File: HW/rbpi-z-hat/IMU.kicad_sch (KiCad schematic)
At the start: 1 part

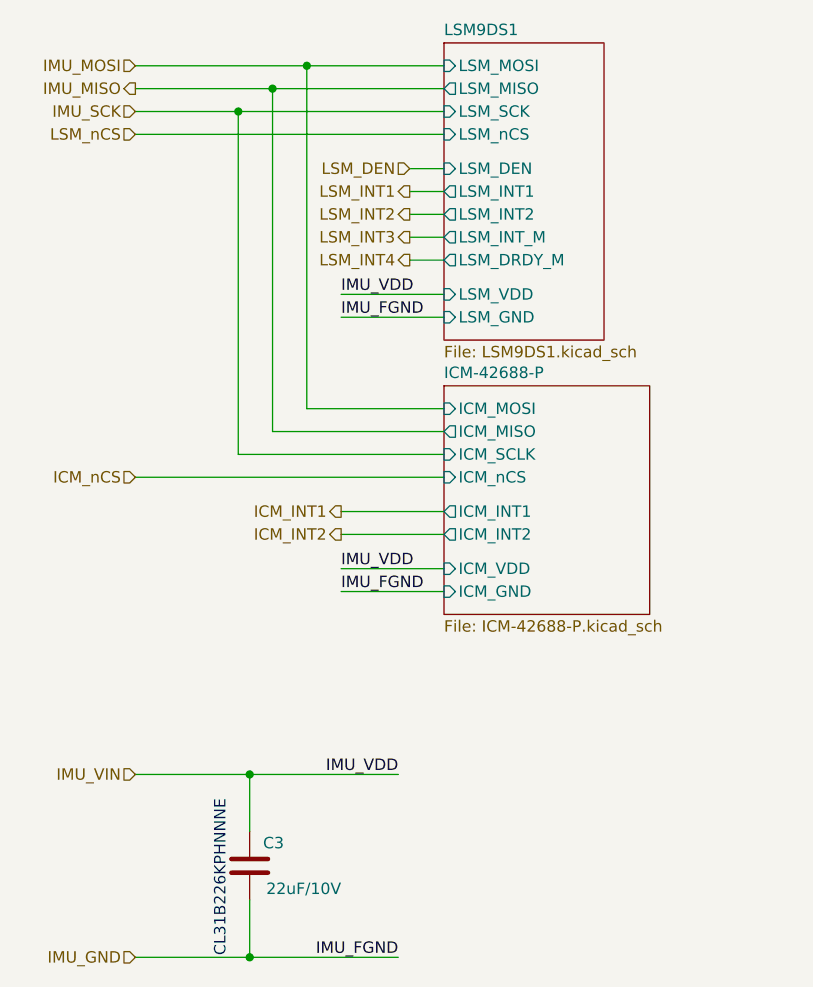
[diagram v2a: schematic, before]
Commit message: Replaced LSM9DS1 with BMI160/QMI8658C
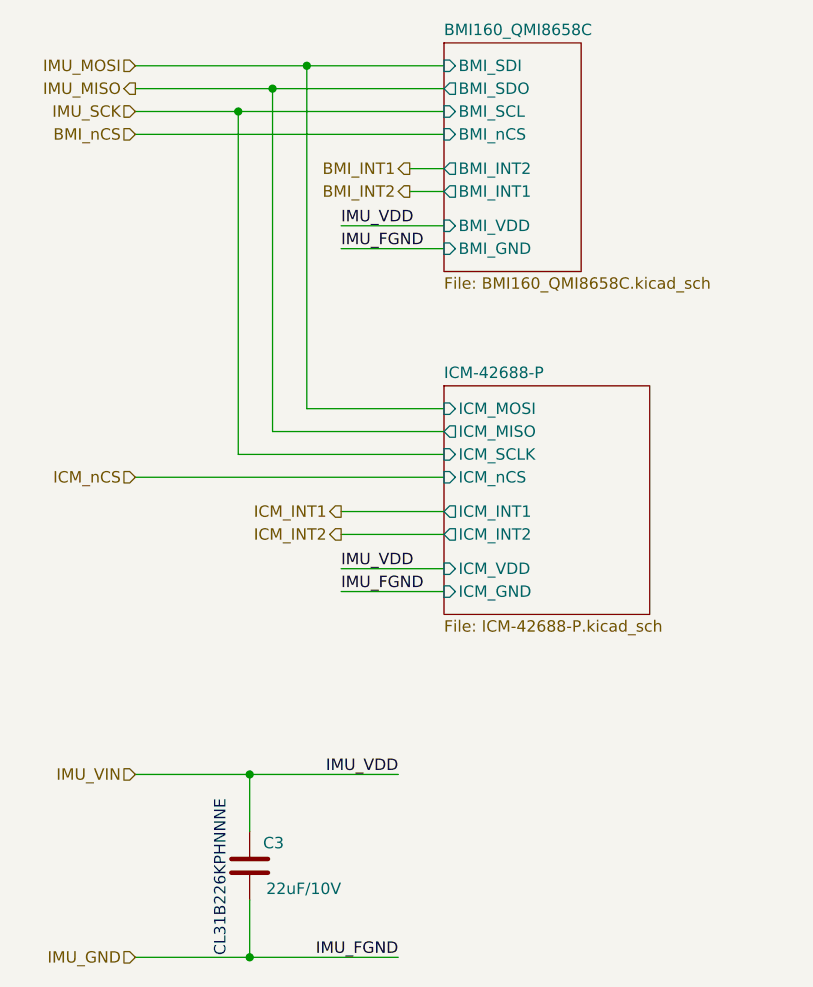
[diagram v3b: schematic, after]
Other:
- removed sheet LSM9DS1
- added sheet BMI160_QMI8658C (BMI160_QMI8658C.kicad_sch)
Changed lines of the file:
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@@
   (junction (at 91.44 182.88) (diameter 0) (color 0 0 0 0)
   )
-  (wire (pts (xy 113.03 105.41) (xy 109.22 105.41))
-    (stroke (width 0) (type default))
-  )
-  (wire (pts (xy 113.03 102.87) (xy 109.22 102.87))
+  (wire (pts (xy 113.03 95.25) (xy 109.22 95.25))
+    (stroke (width 0) (type default))
+  )
+  (wire (pts (xy 113.03 121.92) (xy 97.79 121.92))
+    (stroke (width 0) (type default))
+  )
+  (wire (pts (xy 101.6 104.14) (xy 113.03 104.14))
+    (stroke (width 0) (type default))
+  )
+  (wire (pts (xy 90.17 88.9) (xy 90.17 127))
+    (stroke (width 0) (type default))
+  )
+  (wire (pts (xy 91.44 182.88) (xy 107.95 182.88))
+    (stroke (width 0) (type default))
+  )
+  (wire (pts (xy 91.44 182.88) (xy 91.44 176.53))
+    (stroke (width 0) (type default))
+  )
+  (wire (pts (xy 113.03 129.54) (xy 78.74 129.54))
+    (stroke (width 0) (type default))
+  )
+  (wire (pts (xy 113.03 135.89) (xy 101.6 135.89))
     (stroke (width 0) (type default))
   )
@@
     (stroke (width 0) (type default))
   )
-  (wire (pts (xy 113.03 121.92) (xy 97.79 121.92))
-    (stroke (width 0) (type default))
-  )
-  (wire (pts (xy 101.6 111.76) (xy 113.03 111.76))
-    (stroke (width 0) (type default))
-  )
-  (wire (pts (xy 90.17 88.9) (xy 90.17 127))
-    (stroke (width 0) (type default))
-  )
-  (wire (pts (xy 91.44 182.88) (xy 107.95 182.88))
-    (stroke (width 0) (type default))
-  )
-  (wire (pts (xy 91.44 182.88) (xy 91.44 176.53))
-    (stroke (width 0) (type default))
-  )
-  (wire (pts (xy 113.03 129.54) (xy 78.74 129.54))
-    (stroke (width 0) (type default))
-  )
-  (wire (pts (xy 113.03 135.89) (xy 101.6 135.89))
-    (stroke (width 0) (type default))
-  )
-  (wire (pts (xy 113.03 95.25) (xy 109.22 95.25))
-    (stroke (width 0) (type default))
-  )
-  (wire (pts (xy 113.03 100.33) (xy 109.22 100.33))
-    (stroke (width 0) (type default))
-  )
   (wire (pts (xy 113.03 86.36) (xy 93.98 86.36))
     (stroke (width 0) (type default))
@@
     (stroke (width 0) (type default))
   )
-  (wire (pts (xy 101.6 109.22) (xy 113.03 109.22))
+  (wire (pts (xy 101.6 101.6) (xy 113.03 101.6))
     (stroke (width 0) (type default))
   )
@@
     (effects (font (size 1.27 1.27)) (justify left bottom))
   )
-  (label "IMU_VDD" (at 101.6 109.22 0) (fields_autoplaced)
+  (label "IMU_VDD" (at 101.6 101.6 0) (fields_autoplaced)
     (effects (font (size 1.27 1.27)) (justify left bottom))
   )
@@
     (effects (font (size 1.27 1.27)) (justify left bottom))
   )
-  (label "IMU_FGND" (at 101.6 111.76 0) (fields_autoplaced)
+  (label "IMU_FGND" (at 101.6 104.14 0) (fields_autoplaced)
     (effects (font (size 1.27 1.27)) (justify left bottom))
   )
@@
     (effects (font (size 1.27 1.27)) (justify left bottom))
   )
-  (hierarchical_label "LSM_INT2" (shape output) (at 109.22 100.33 180) (fields_autoplaced)
-    (effects (font (size 1.27 1.27)) (justify right))
-  )
-  (hierarchical_label "LSM_INT4" (shape output) (at 109.22 105.41 180) (fields_autoplaced)
-    (effects (font (size 1.27 1.27)) (justify right))
-  )
-  (hierarchical_label "LSM_DEN" (shape input) (at 109.22 95.25 180) (fields_autoplaced)
-    (effects (font (size 1.27 1.27)) (justify right))
-  )
-  (hierarchical_label "LSM_INT1" (shape output) (at 109.22 97.79 180) (fields_autoplaced)
+  (hierarchical_label "BMI_INT2" (shape output) (at 109.22 97.79 180) (fields_autoplaced)
+    (effects (font (size 1.27 1.27)) (justify right))
+  )
+  (hierarchical_label "BMI_INT1" (shape output) (at 109.22 95.25 180) (fields_autoplaced)
     (effects (font (size 1.27 1.27)) (justify right))
   )
@@
     (effects (font (size 1.27 1.27)) (justify right))
   )
-  (hierarchical_label "LSM_nCS" (shape input) (at 78.74 91.44 180) (fields_autoplaced)
-    (effects (font (size 1.27 1.27)) (justify right))
-  )
-  (hierarchical_label "LSM_INT3" (shape output) (at 109.22 102.87 180) (fields_autoplaced)
+  (hierarchical_label "BMI_nCS" (shape input) (at 78.74 91.44 180) (fields_autoplaced)
     (effects (font (size 1.27 1.27)) (justify right))
   )
@@
     )
   )
-  (sheet (at 113.03 81.28) (size 17.78 33.02) (fields_autoplaced)
-    (stroke (width 0) (type solid))
-    (fill (color 0 0 0 0.0000))
-    (property "Sheetname" "LSM9DS1" (at 113.03 80.5684 0)
-      (effects (font (size 1.27 1.27)) (justify left bottom))
-    )
-    (property "Sheetfile" "LSM9DS1.kicad_sch" (at 113.03 114.8846 0)
-      (effects (font (size 1.27 1.27)) (justify left top))
-    )
-    (pin "LSM_SCK" input (at 113.03 88.9 180)
-      (effects (font (size 1.27 1.27)) (justify left))
-    )
-    (pin "LSM_INT1" output (at 113.03 97.79 180)
-      (effects (font (size 1.27 1.27)) (justify left))
-    )
-    (pin "LSM_INT2" output (at 113.03 100.33 180)
-      (effects (font (size 1.27 1.27)) (justify left))
-    )
-    (pin "LSM_DEN" input (at 113.03 95.25 180)
-      (effects (font (size 1.27 1.27)) (justify left))
-    )
-    (pin "LSM_nCS" input (at 113.03 91.44 180)
-      (effects (font (size 1.27 1.27)) (justify left))
-    )
-    (pin "LSM_INT_M" output (at 113.03 102.87 180)
-      (effects (font (size 1.27 1.27)) (justify left))
-    )
-    (pin "LSM_DRDY_M" output (at 113.03 105.41 180)
-      (effects (font (size 1.27 1.27)) (justify left))
-    )
-    (pin "LSM_MOSI" input (at 113.03 83.82 180)
-      (effects (font (size 1.27 1.27)) (justify left))
-    )
-    (pin "LSM_MISO" output (at 113.03 86.36 180)
-      (effects (font (size 1.27 1.27)) (justify left))
-    )
-    (pin "LSM_VDD" input (at 113.03 109.22 180)
-      (effects (font (size 1.27 1.27)) (justify left))
-    )
-    (pin "LSM_GND" input (at 113.03 111.76 180)
-      (effects (font (size 1.27 1.27)) (justify left))
-    )
-    (instances
-      (project "rbpi-z-hat"
-        (path "/d99b0340-d795-4b40-9cde-9851c6cee99d/00000000-0000-0000-0000-00005ee06f22" (page "7"))
-      )
-    )
-  )
   (sheet (at 113.03 119.38) (size 22.86 25.4) (fields_autoplaced)
     (stroke (width 0) (type solid))
@@
       )
     )
+  )
+  (sheet (at 113.03 81.28) (size 15.24 25.4) (fields_autoplaced)
+    (stroke (width 0.1524) (type solid))
+    (fill (color 0 0 0 0.0000))
+    (property "Sheetname" "BMI160_QMI8658C" (at 113.03 80.5684 0)
+      (effects (font (size 1.27 1.27)) (justify left bottom))
+    )
+    (property "Sheetfile" "BMI160_QMI8658C.kicad_sch" (at 113.03 107.2646 0)
+      (effects (font (size 1.27 1.27)) (justify left top))
+    )
+    (pin "BMI_VDD" input (at 113.03 101.6 180)
+      (effects (font (size 1.27 1.27)) (justify left))
+    )
+    (pin "BMI_GND" input (at 113.03 104.14 180)
+      (effects (font (size 1.27 1.27)) (justify left))
+    )
+    (pin "BMI_INT1" output (at 113.03 97.79 180)
+      (effects (font (size 1.27 1.27)) (justify left))
+    )
+    (pin "BMI_INT2" output (at 113.03 95.25 180)
+      (effects (font (size 1.27 1.27)) (justify left))
+    )
+    (pin "BMI_SDO" output (at 113.03 86.36 180)
+      (effects (font (size 1.27 1.27)) (justify left))
+    )
+    (pin "BMI_nCS" input (at 113.03 91.44 180)
+      (effects (font (size 1.27 1.27)) (justify left))
+    )
+    (pin "BMI_SCL" input (at 113.03 88.9 180)
+      (effects (font (size 1.27 1.27)) (justify left))
+    )
+    (pin "BMI_SDI" input (at 113.03 83.82 180)
+      (effects (font (size 1.27 1.27)) (justify left))
+    )
+    (instances
+      (project "rbpi-z-hat"
+        (path "/d99b0340-d795-4b40-9cde-9851c6cee99d/00000000-0000-0000-0000-00005ee06f22" (page "20"))
+      )
+    )

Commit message: Changes in Sch & PCB
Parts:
- C3: footprint Capacitor_SMD:C_1206_3216Metric -> Capacitor_SMD:C_0805_2012Metric
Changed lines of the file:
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@@
       (effects (font (size 1.27 1.27)) (justify left))
     )
-    (property "Footprint" "Capacitor_SMD:C_1206_3216Metric" (at 90.4748 176.53 0)
+    (property "Footprint" "Capacitor_SMD:C_0805_2012Metric" (at 90.4748 176.53 0)
       (effects (font (size 1.27 1.27)) hide)
     )
